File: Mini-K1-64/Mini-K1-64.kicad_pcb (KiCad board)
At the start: 2 copper layers, 55 x 44 mm, 48 parts, among them J1 USB_C_Receptacle_USB2.0_14P, J3 Conn_01x16_Pin, J4 Conn_01x16_Pin, J5 Conn_01x16_Pin, J6 Conn_01x16_Pin, SW1 KEY, U1 CH340N, U2 FS32K144HAT0MLHT, U3 AMS1117-3.3, Y1 8M

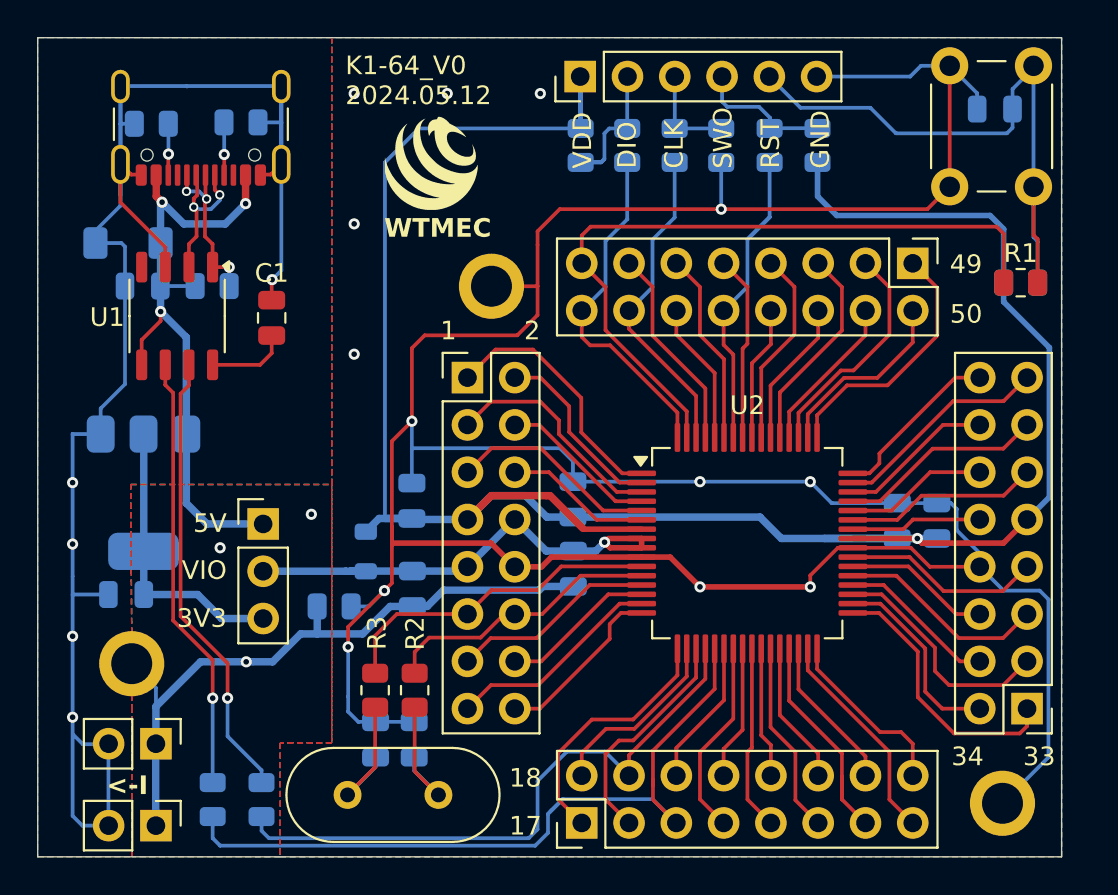
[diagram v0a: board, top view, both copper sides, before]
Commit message: Update Debug Connector
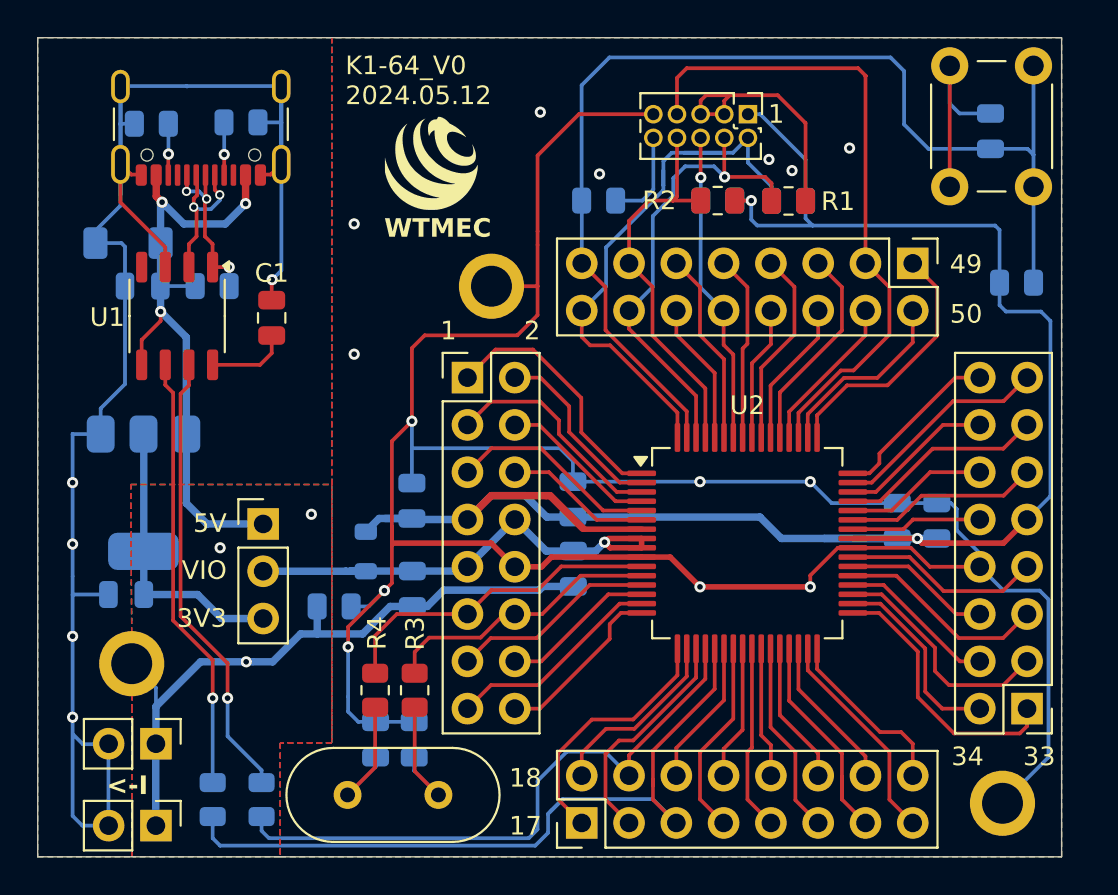
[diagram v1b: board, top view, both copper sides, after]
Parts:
- removed the R1 at (167.0, 92.8)
- removed the R4 at (145.8, 85.5)
- removed the R7 at (153.5, 85.5)
- added R2: 10K, Resistor_SMD:R_0805_2012Metric, F.Cu at (150.7, 88.4)
- J2: footprint Connector_PinHeader_2.54mm:PinHeader_1x06_P2.54mm_Vertical -> Connector_PinHeader_1.27mm:PinHeader_2x05_P1.27mm_Vertical
- R1: renamed from R6; moved to F.Cu
- moved R6 11.6 mm to (154.5, 88.4), turned to 180 degrees
- moved J2 9.23 mm to (152.3, 83.8), turned to -90 degrees
- moved R7 6.13 mm to (150.7, 88.4), turned to 180 degrees
- moved R5 5.05 mm to (144.3, 88.4), turned to 0 degrees
- moved R1 4.69 mm to (154.5, 88.4), turned to 0 degrees
- moved C2 1.21 mm to (165.3, 84.7), turned to 90 degrees
- moved R10 0.22 mm to (166.7, 92.8)
- renumbered R12 to R10, R13 to R11, R14 to R12, R15 to R13, R16 to R14, R2 to R3, R3 to R4, R8 to R6, R9 to R7, R10 to R8, R11 to R9
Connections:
- C2 pad 1: /MCU/RESET -> /MCU/PTA5
- J2 pad 2: /JTAG/SWDIO -> /MCU/PTA4
- J2 pad 3: /JTAG/SWCLK -> GNDD
- J2 pad 4: /JTAG/SWO -> /MCU/PTC4
- J2 pad 5: /MCU/RESET -> GNDD
- J2 pad 6: GNDD -> /MCU/PTA10
- R1 pad 1: /JTAG/SWCLK -> /MCU/PTC4
- R10 pad 2: /MCU/RESET -> /MCU/PTA5
- R5 pad 1: /JTAG/SWCLK -> /MCU/PTA5
- R5 pad 2: /MCU/PTC4 -> Net-(J2-RESET)
- R6 pad 2: /JTAG/SWDIO -> /MCU/PTA4
- R7 pad 2: /JTAG/SWO -> /MCU/PTA10
- SW1 pad 2: /MCU/RESET -> /MCU/PTA5
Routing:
- net /MCU/RESET: track 35.2 -> 0.00 mm
- net VDD: track 127.6 -> 101.6 mm, vias 1 -> 2
- net /MCU/PTA5: track 38.8 -> 61.7 mm
- net /MCU/PTC7: track 12.3 -> 34.9 mm
- net /MCU/PTA4: track 18.6 -> 31.4 mm
- net /MCU/PTC5: track 11.1 -> 21.1 mm
- net /JTAG/SWDIO: track 8.20 -> 0.00 mm
- net /MCU/PTC4: track 17.3 -> 25.4 mm, vias 0 -> 1
- net /JTAG/SWO: track 7.39 -> 0.00 mm
- net GNDD: track 174.7 -> 167.8 mm, vias 13 -> 14
- net /JTAG/SWCLK: track 5.29 -> 0.00 mm
- net Net-(J2-RESET): track 0.00 -> 5.05 mm
- net /MCU/PTA10: track 17.7 -> 16.8 mm, vias 0 -> 1
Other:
- board text removed: "CLK"
- board text removed: "DIO"
- board text removed: "GND"
- board text removed: "RST"
- board text removed: "SWO"
- board text removed: "VDD"

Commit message: Update to Kicad 9
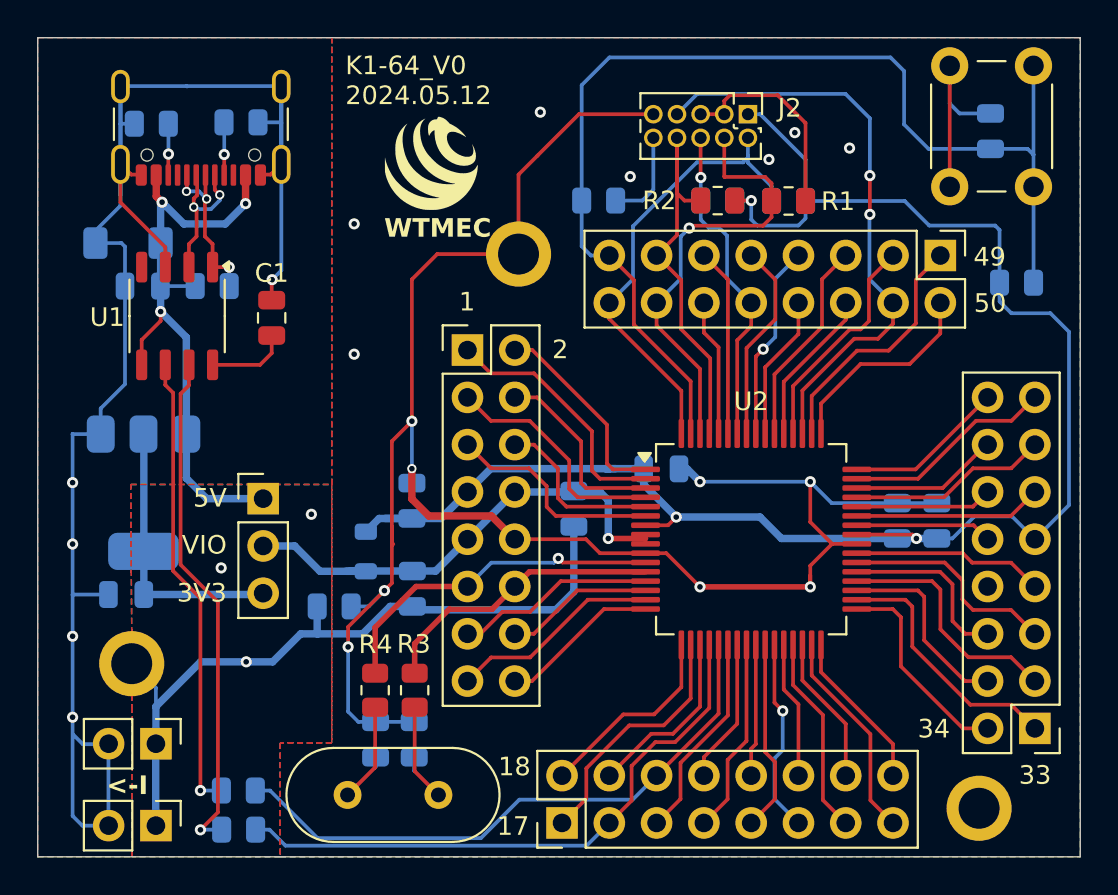
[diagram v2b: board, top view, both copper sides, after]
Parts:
- moved C6 5.03 mm to (147.7, 102.8), turned to 0 degrees
- moved C5 3.23 mm to (143.0, 105.0)
- moved H2 2.26 mm to (140.0, 91.3)
- moved R13 2.03 mm to (125.0, 122.2), turned to 0 degrees
- moved J4 1.54 mm to (162.6, 91.4)
- moved J3 1.48 mm to (137.2, 96.5)
- moved R14 1.46 mm to (124.9, 120.1), turned to 0 degrees
- moved JP1 1.36 mm to (126.3, 104.4)
- moved H3 1.29 mm to (164.7, 121.1)
- moved J6 1.14 mm to (167.7, 116.8)
- moved J5 1.06 mm to (142.3, 121.9)
- moved U2 0.30 mm to (152.5, 106.6)
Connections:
- J3 pad 1: /MCU/PTD1 -> /MCU/PTD0
- J3 pad 2: /MCU/PTD0 -> /MCU/PTD1
- J3 pad 3: /MCU/PTE11 -> /MCU/PTE10
- J3 pad 4: /MCU/PTE10 -> /MCU/PTE11
- J3 pad 5: /MCU/PTE5 -> /MCU/PTE4
- J3 pad 6: /MCU/PTE4 -> /MCU/PTE5
- J4 pad 1: /MCU/PTA1 -> /MCU/PTA0
- J4 pad 2: /MCU/PTA0 -> /MCU/PTA1
- J4 pad 3: /MCU/PTC7 -> /MCU/PTC6
- J4 pad 4: /MCU/PTC6 -> /MCU/PTC7
- J4 pad 5: /MCU/PTE6 -> /MCU/PTE2
- J4 pad 6: /MCU/PTE2 -> /MCU/PTE6
- J4 pad 7: /MCU/PTA13 -> /MCU/PTA12
- J4 pad 8: /MCU/PTA12 -> /MCU/PTA13
- J5 pad 1: /MCU/PTE8 -> /MCU/PTB5
- J5 pad 10: /MCU/PTC0 -> /MCU/PTC1
- J5 pad 2: /MCU/PTB5 -> /MCU/PTE8
- J5 pad 3: /MCU/PTB4 -> /MCU/PTC3
- J5 pad 4: /MCU/PTC3 -> /MCU/PTB4
- J5 pad 5: /MCU/PTC2 -> /MCU/PTD7
- J5 pad 6: /MCU/PTD7 -> /MCU/PTC2
- J5 pad 7: /MCU/PTD6 -> /MCU/PTD5
- J5 pad 8: /MCU/PTD5 -> /MCU/PTD6
- J5 pad 9: /MCU/PTC1 -> /MCU/PTC0
- J6 pad 1: /MCU/PTB1 -> /MCU/PTB0
- J6 pad 2: /MCU/PTB0 -> /MCU/PTB1
- J6 pad 3: /MCU/PTC9 -> /MCU/PTC8
- J6 pad 4: /MCU/PTC8 -> /MCU/PTC9
- J6 pad 5: /MCU/PTA7 -> /MCU/PTA6
- J6 pad 6: /MCU/PTA6 -> /MCU/PTA7
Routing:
- net GNDD: track 167.8 -> 126.3 mm, vias 14 -> 15
- net VDD: track 101.6 -> 91.8 mm, vias 2 -> 3
- net /MCU/PTC2: track 41.2 -> 32.4 mm
- net /MCU/PTA4: track 31.4 -> 25.0 mm
- net /MCU/PTC8: track 8.51 -> 13.0 mm
- net /MCU/PTE10: track 8.51 -> 12.7 mm
- net /MCU/PTE4: track 7.90 -> 11.8 mm
- net /MCU/PTA6: track 7.88 -> 11.8 mm
- net /MCU/PTD0: track 9.96 -> 13.7 mm
- net /MCU/PTC6: track 8.51 -> 12.1 mm
- net /MCU/PTB5: track 10.0 -> 13.5 mm
- net /MCU/PTB1: track 14.6 -> 11.2 mm
- net /MCU/PTC0: track 7.03 -> 10.3 mm
- net /MCU/PTD5: track 7.24 -> 10.5 mm
- net /MCU/PTD7: track 7.88 -> 11.2 mm
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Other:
- board size 55 x 44 mm -> 56 x 44 mm
